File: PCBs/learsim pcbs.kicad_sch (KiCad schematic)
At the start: 51 parts, among them SW1 MHz, SW2 KHz, SW3 2MS1T1B1M2QES-5, U1 ESP32-C6-DEV-KIT-N8, U2 MAX7219, U3 MAX7219

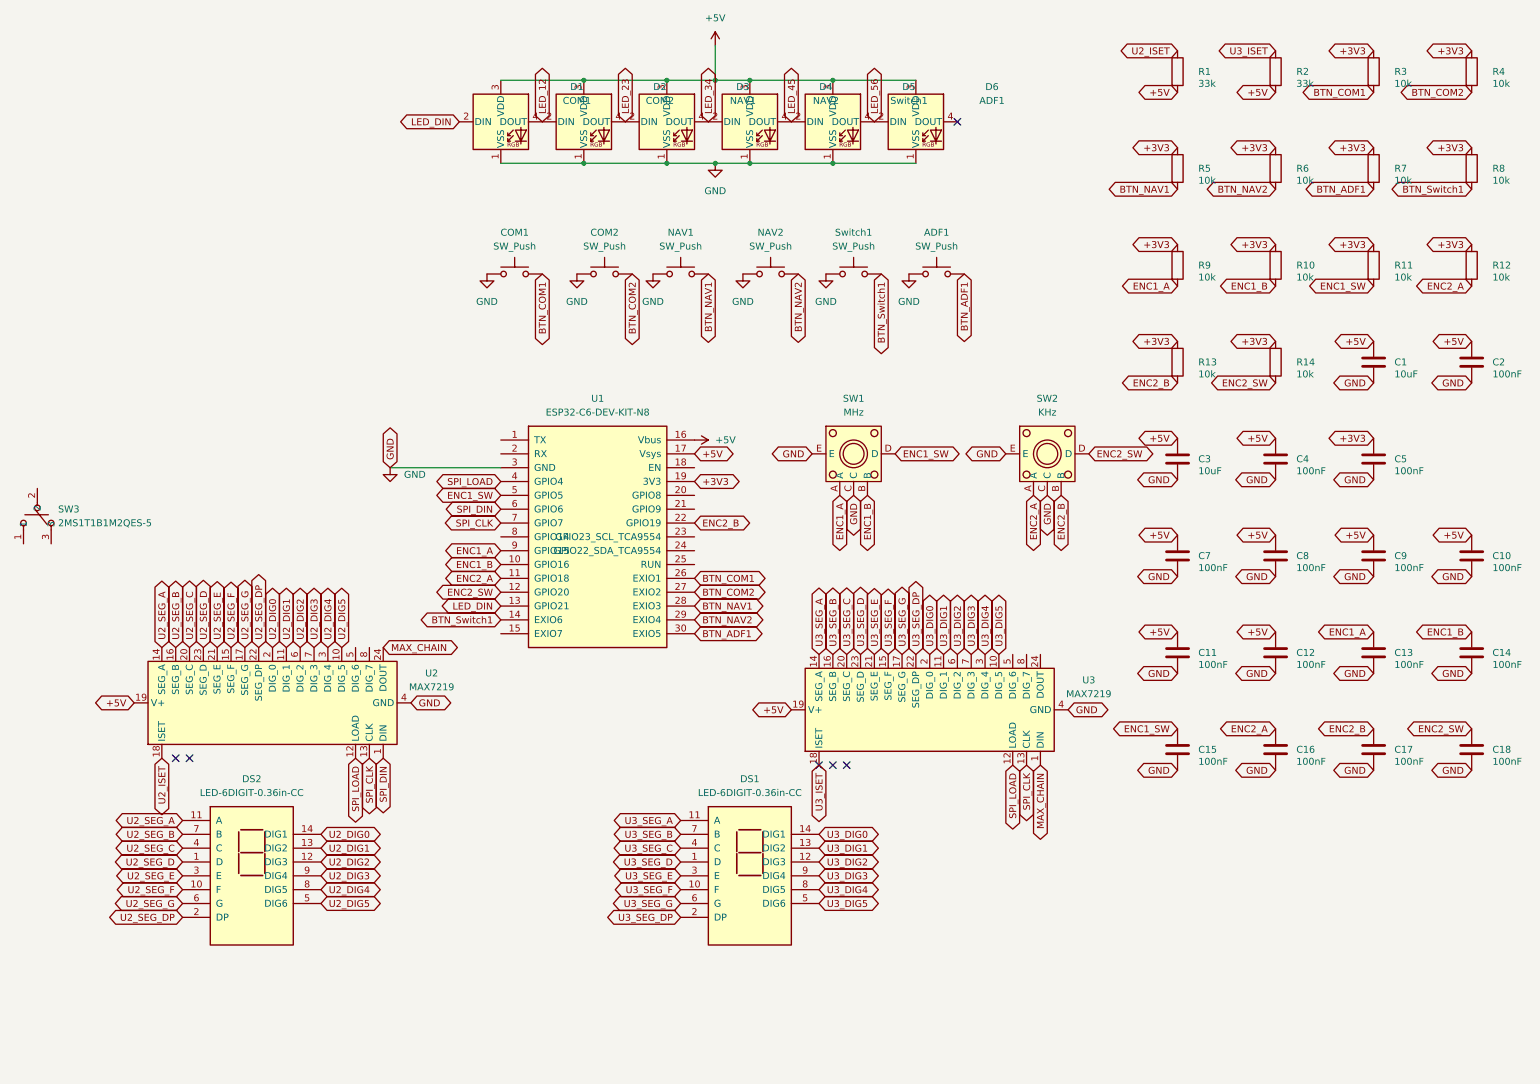
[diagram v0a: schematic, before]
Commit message: Wire SW3 SPDT toggle to the ESP32
Wire the newly-added SW3 (2MS1T1B1M2QES-5) toggle switch:
- pin 2 (common pole) -> GND
- pin 1 -> GPIO8 (SW3_A), with 10k pull-up R15 to +3V3
- pin 3 -> GPIO9 (SW3_B), with 10k pull-up R16 to +3V3

Each throw reads LOW when selected, HIGH via pull-up otherwise, so both
positions (and a centre-off state, if any) are distinguishable in firmware.
R15/R16 use the THT axial footprint to match this iteration. README GPIO map
updated. Verified: SW3/R15/R16 nets resolve correctly, 0 floating pins.

Co-Authored-By: Claude Opus 4.8 <noreply@anthropic.com>
Claude-Session: https://claude.ai/code/session_01PYVnDFXSTkVYnSG662sK4G
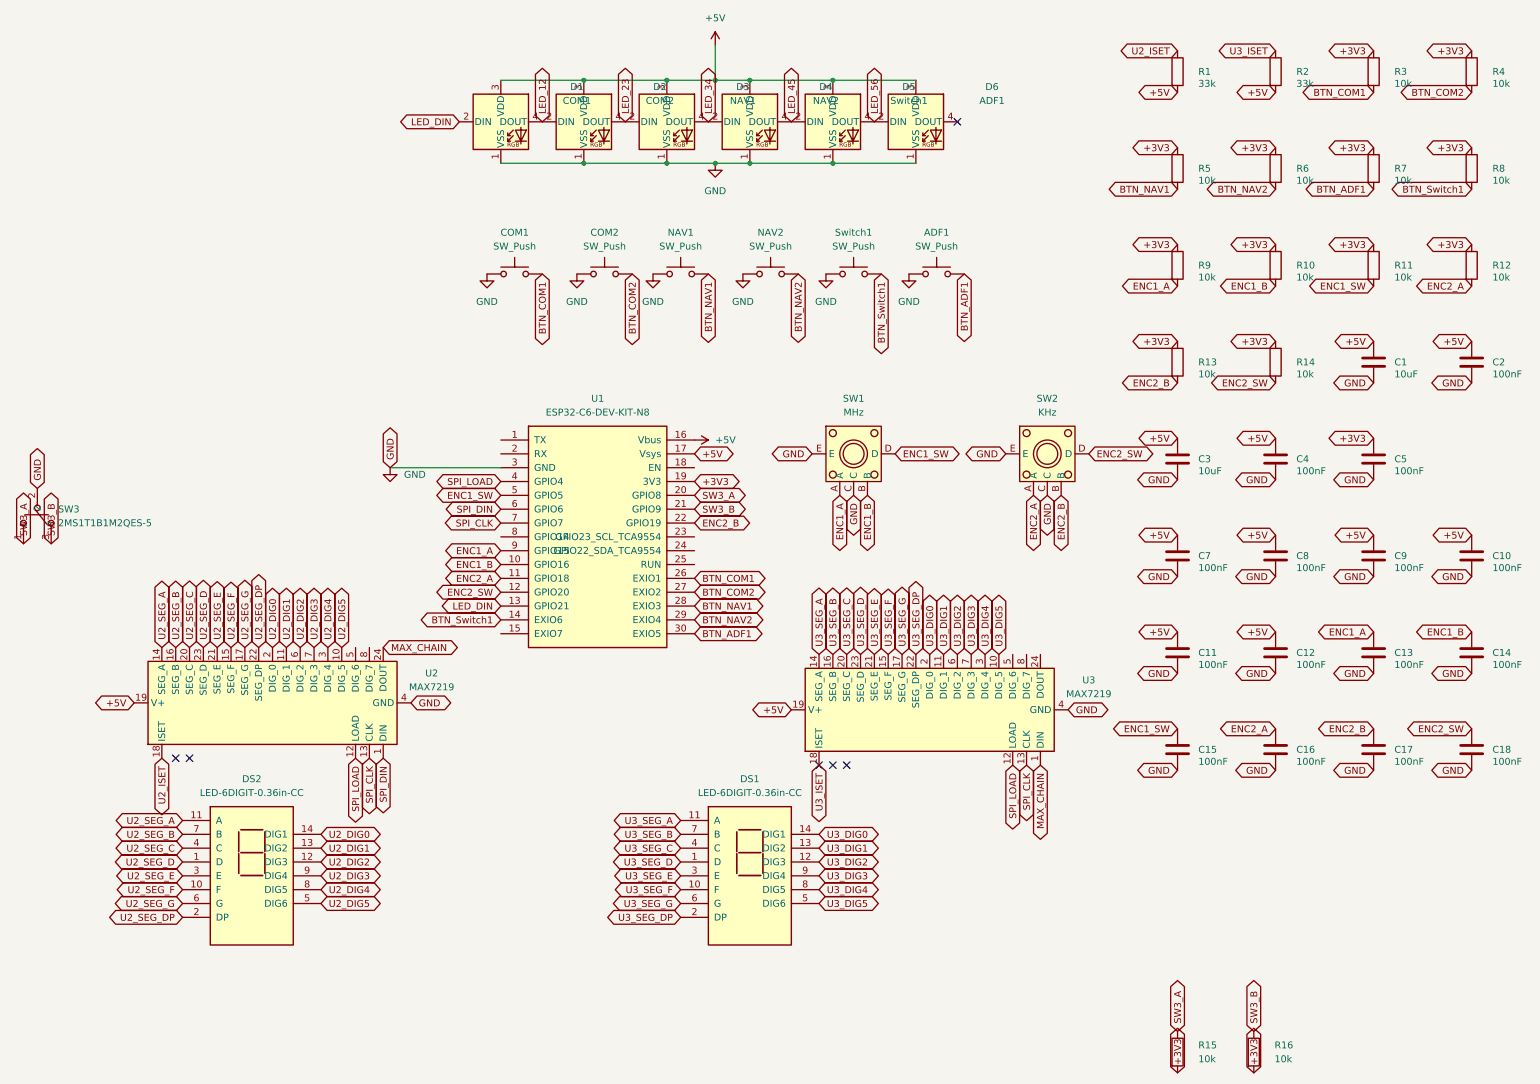
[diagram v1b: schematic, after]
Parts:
- added R15, R16: 10k, Resistor_THT:R_Axial_DIN0207_L6.3mm_D2.5mm_P7.62mm_Horizontal, symbol Device:R
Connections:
- net +3V3: now also R15.2, R16.2
- net GND: now also SW3.2
- net SW3_A: now reaches SW3.1
- net SW3_A: now also U1.20 (GPIO8), R15.1
- net SW3_B: now reaches SW3.3
- net SW3_B: now also U1.21 (GPIO9), R16.1
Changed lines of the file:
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@@
 		)
+	)
+	(symbol
+		(lib_id "Device:R")
+		(at 236.0 200.0 0)
+		(unit 1)
+		(body_style 1)
+		(exclude_from_sim no)
+		(in_bom yes)
+		(on_board yes)
+		(in_pos_files yes)
+		(dnp no)
+		(property "Reference" "R15"
+			(at 239.81 198.73 0)
+			(effects (font (size 1.27 1.27)) (justify left))
+		)
+		(property "Value" "10k"
+			(at 239.81 201.27 0)
+			(effects (font (size 1.27 1.27)) (justify left))
+		)
+		(property "Footprint" "Resistor_THT:R_Axial_DIN0207_L6.3mm_D2.5mm_P7.62mm_Horizontal"
+			(at 236.0 200.0 0)
+			(hide yes)
+			(effects (font (size 1.27 1.27)))
+		)
+		(property "Datasheet" "~"
+			(at 236.0 200.0 0)
+			(hide yes)
+			(effects (font (size 1.27 1.27)))
+		)
+		(pin "1"
+		)
+		(pin "2"
+		)
+		(instances
+			(project "learsim pcbs"
+				(path "/27520048-f2d9-41fa-a766-14782a208ac0"
+					(reference "R15")
+					(unit 1)
+				)
+			)
+		)
+	)
+	(symbol
+		(lib_id "Device:R")
+		(at 250.0 200.0 0)
+		(unit 1)
+		(body_style 1)
+		(exclude_from_sim no)
+		(in_bom yes)
+		(on_board yes)
+		(in_pos_files yes)
+		(dnp no)
+		(property "Reference" "R16"
+			(at 253.81 198.73 0)
+			(effects (font (size 1.27 1.27)) (justify left))
+		)
+		(property "Value" "10k"
+			(at 253.81 201.27 0)
+			(effects (font (size 1.27 1.27)) (justify left))
+		)
+		(property "Footprint" "Resistor_THT:R_Axial_DIN0207_L6.3mm_D2.5mm_P7.62mm_Horizontal"
+			(at 250.0 200.0 0)
+			(hide yes)
+			(effects (font (size 1.27 1.27)))
+		)
+		(property "Datasheet" "~"
+			(at 250.0 200.0 0)
+			(hide yes)
+			(effects (font (size 1.27 1.27)))
+		)
+		(pin "1"
+		)
+		(pin "2"
+		)
+		(instances
+			(project "learsim pcbs"
+				(path "/27520048-f2d9-41fa-a766-14782a208ac0"
+					(reference "R16")
+					(unit 1)
+				)
+			)
+		)
+	)
+	(global_label "GND"
+		(shape bidirectional)
+		(at 26.67 96.52 90)
+		(fields_autoplaced yes)
+		(effects (font (size 1.27 1.27)) (justify left))
+	)
+	(global_label "SW3_A"
+		(shape bidirectional)
+		(at 24.13 106.68 270)
+		(fields_autoplaced yes)
+		(effects (font (size 1.27 1.27)) (justify left))
+	)
+	(global_label "SW3_A"
+		(shape bidirectional)
+		(at 147.32 97.79 0)
+		(fields_autoplaced yes)
+		(effects (font (size 1.27 1.27)) (justify left))
+	)
+	(global_label "SW3_A"
+		(shape bidirectional)
+		(at 236.0 196.19 90)
+		(fields_autoplaced yes)
+		(effects (font (size 1.27 1.27)) (justify left))
+	)
+	(global_label "SW3_B"
+		(shape bidirectional)
+		(at 29.21 106.68 270)
+		(fields_autoplaced yes)
+		(effects (font (size 1.27 1.27)) (justify left))
+	)
+	(global_label "SW3_B"
+		(shape bidirectional)
+		(at 147.32 100.33 0)
+		(fields_autoplaced yes)
+		(effects (font (size 1.27 1.27)) (justify left))
+	)
+	(global_label "SW3_B"
+		(shape bidirectional)
+		(at 250.0 196.19 90)
+		(fields_autoplaced yes)
+		(effects (font (size 1.27 1.27)) (justify left))
+	)
+	(global_label "+3V3"
+		(shape bidirectional)
+		(at 236.0 203.81 270)
+		(fields_autoplaced yes)
+		(effects (font (size 1.27 1.27)) (justify left))
+	)
+	(global_label "+3V3"
+		(shape bidirectional)
+		(at 250.0 203.81 270)
+		(fields_autoplaced yes)
+		(effects (font (size 1.27 1.27)) (justify left))
 	)
 	(sheet_instances
